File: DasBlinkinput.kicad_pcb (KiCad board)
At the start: 4 copper layers, 25.4 x 50.8 mm, 34 parts, among them P101 CONN_01X02, P102 CONN_01X01, P103 CONN_01X01, P104 CONN_01X01, P105 CONN_01X05, P201 CONN_01X01, P301 CONN_01X01, P401 CONN_01X01, P501 CONN_01X01, U101 LP2980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

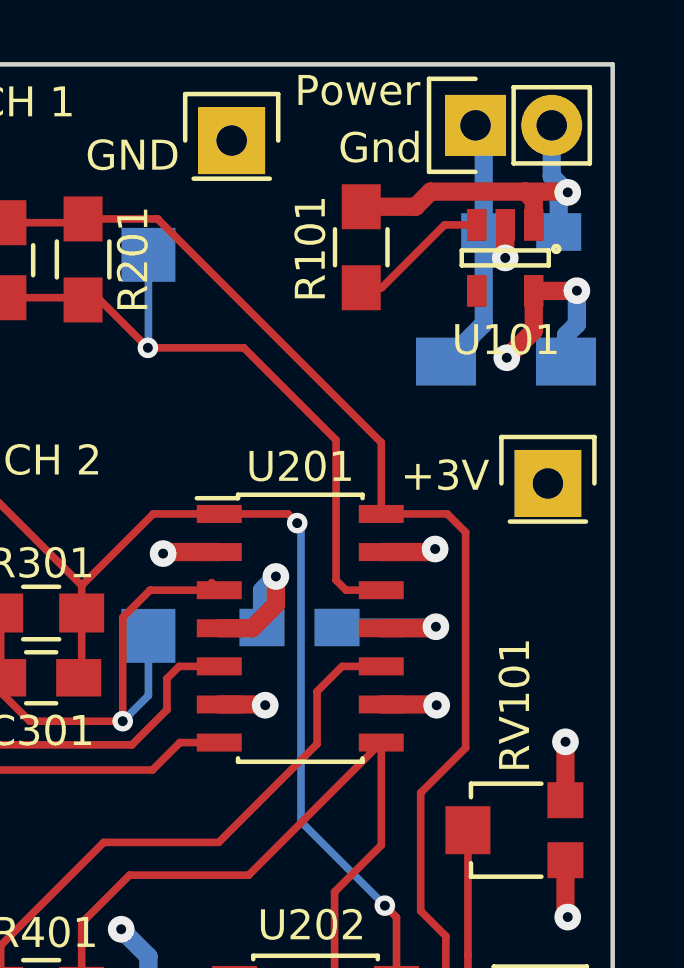
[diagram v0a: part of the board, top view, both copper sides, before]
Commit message: adjust layout of power section
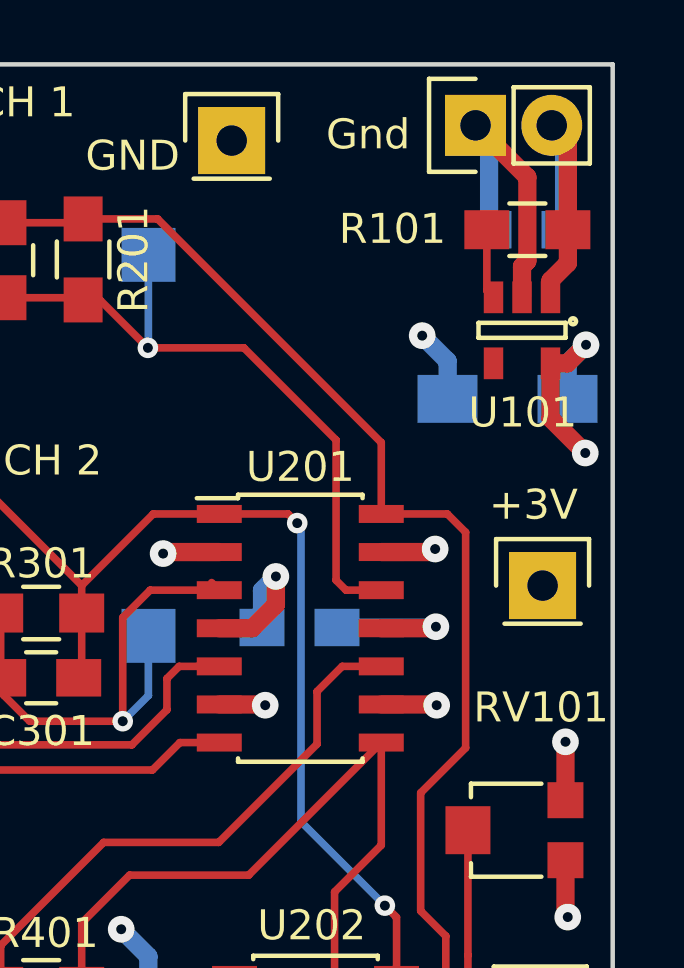
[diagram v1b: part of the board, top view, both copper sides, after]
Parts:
- moved R101 5.57 mm to (153.1, 71.3), turned to 0 degrees
- moved P102 3.41 mm to (153.6, 83.2)
- moved U101 2.48 mm to (152.9, 74.7)
- moved C102 1.25 mm to (152.5, 76.9)
- moved C101 0.19 mm to (153.1, 71.3)
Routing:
- net GND: track 38.5 -> 41.5 mm
- net Net-(C101-Pad1): track 12.2 -> 9.84 mm, vias 1 -> 0
- net Net-(R101-Pad1): track 4.72 -> 2.34 mm

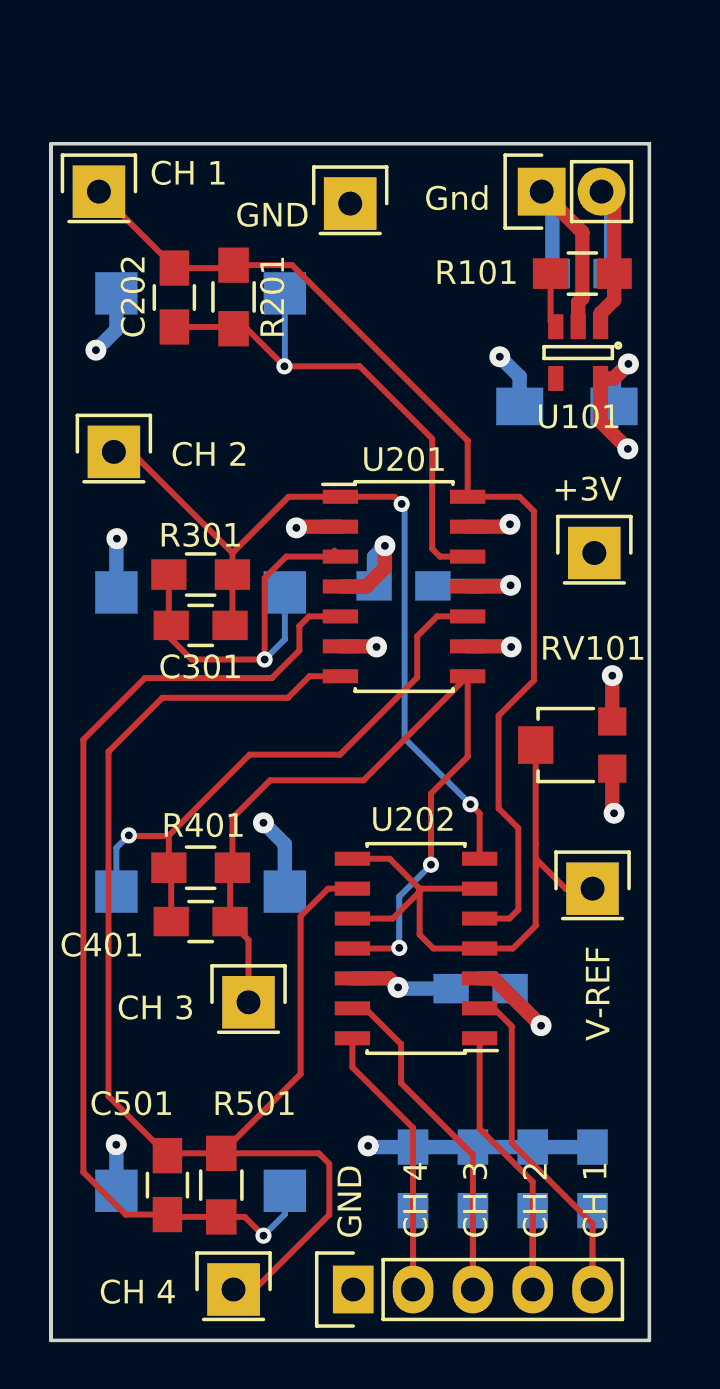
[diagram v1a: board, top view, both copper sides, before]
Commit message: corrected inputs on opamp and rerouted traces
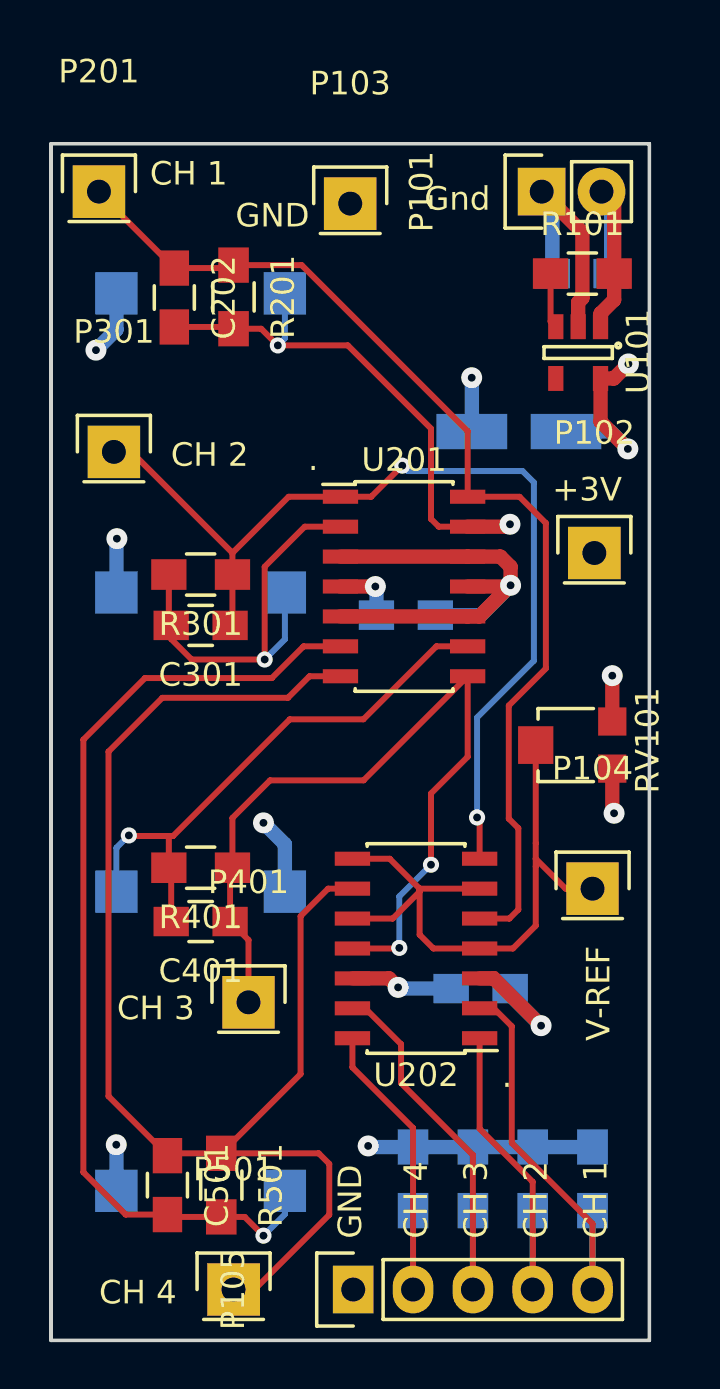
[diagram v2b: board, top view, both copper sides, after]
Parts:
- C102: footprint Capacitors_SMD:C_1206_HandSoldering -> Capacitors_Tantalum_SMD:TantalC_SizeA_EIA-3216_HandSoldering
- U201, U202: footprint Housings_SOIC:SOIC-14_3.9x8.7mm_Pitch1.27mm -> DasBlinkinput:SOIC-14_3.9x8.7mm_Pitch1.27mm
- moved C102 2.30 mm to (150.4, 78.0)
- moved C201 1.25 mm to (145.6, 85.8), turned to 180 degrees
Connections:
- C201 pad 1: +3V -> GND
- C201 pad 2: GND -> +3V
- U201 pad 10: Net-(C401-Pad2) -> GND
- U201 pad 12: Net-(C202-Pad2) -> GND
- U201 pad 13: GND -> Net-(C202-Pad2)
- U201 pad 2: GND -> Net-(C301-Pad2)
- U201 pad 3: Net-(C301-Pad2) -> GND
- U201 pad 5: Net-(C501-Pad2) -> GND
- U201 pad 6: GND -> Net-(C501-Pad2)
- U201 pad 9: GND -> Net-(C401-Pad2)
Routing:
- net GND: track 41.5 -> 51.3 mm, vias 12 -> 8
- net Net-(C301-Pad1): track 36.0 -> 42.9 mm
- net Net-(C401-Pad2): track 26.2 -> 24.0 mm
- net Net-(C501-Pad2): track 43.8 -> 42.0 mm
- net +3V: track 29.1 -> 27.6 mm
- net Net-(C202-Pad2): track 22.3 -> 22.4 mm, vias 1 -> 2

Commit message: arranged silkscreen labels and generated gerbers
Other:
- board text added: "DasBlinkInput Rev. 1"
- board text removed: "DasBlinkInput Rev. 0"

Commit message: final revised design
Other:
- rule pad_to_mask_clearance: 0.2 -> 0.0508
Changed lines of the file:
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@@
     (2 GND.Cu signal)
     (31 B.Cu signal)
-    (32 B.Adhes user)
-    (33 F.Adhes user)
-    (34 B.Paste user hide)
-    (35 F.Paste user hide)
+    (32 B.Adhes user hide)
+    (33 F.Adhes user hide)
+    (34 B.Paste user)
+    (35 F.Paste user)
     (36 B.SilkS user)
     (37 F.SilkS user)
-    (38 B.Mask user hide)
+    (38 B.Mask user)
     (39 F.Mask user)
     (40 Dwgs.User user)
@@
     (pad_size 1.524 1.524)
     (pad_drill 0.762)
-    (pad_to_mask_clearance 0.2)
+    (pad_to_mask_clearance 0.0508)
+    (solder_mask_min_width 0.1016)
     (aux_axis_origin 0 0)
     (visible_elements FFFEFF7F)
